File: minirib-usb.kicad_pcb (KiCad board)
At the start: 2 copper layers, 49.5 x 22.5 mm, 56 parts, among them J1 USB_B_Micro, J2 SB9600 Out, Q1 MMST3904-7-F, Q2 MMST3906-7-F, Q3 MMST3906-7-F, Q4 MMST3904-7-F, Q5 MMST3904-7-F, Q6 MMST3904-7-F, Q7 MMST3904-7-F, Q8 MMST3906-7-F, Q9 MMST3906-7-F, U1 CH340G, U2 TL081H, Y1 12MHz

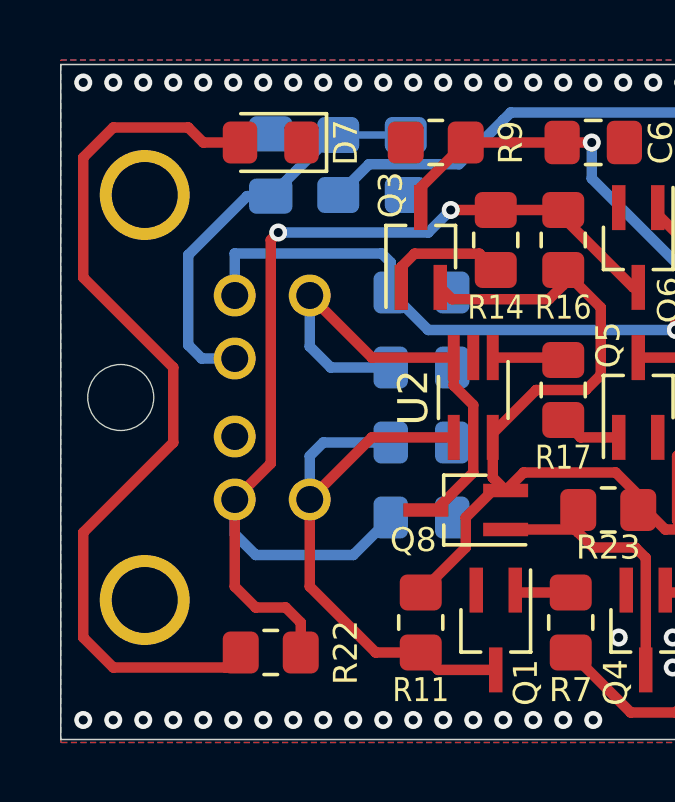
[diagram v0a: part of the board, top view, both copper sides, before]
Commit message: schematic fixes based on rev B testing
- switched Opamp to MCP6491T to use correct footprint (SC70 footprint for TL081H is incorrect)
- Removed D7 BUSY LED as it was interfering with the proper signalling on the BUSY line
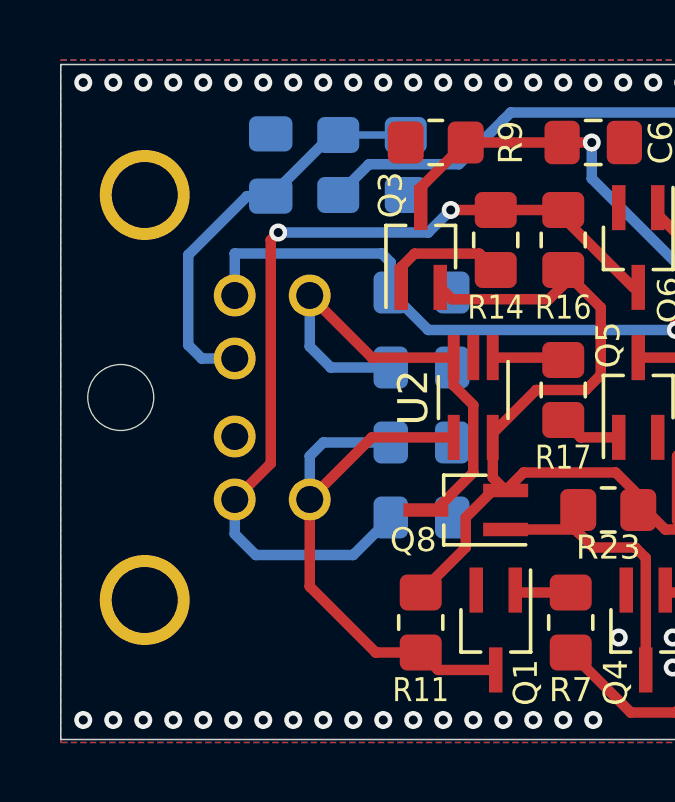
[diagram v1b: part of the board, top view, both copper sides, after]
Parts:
- removed D7: DLED, Diode_SMD:D_0805_2012Metric_Pad1.15x1.40mm_HandSolder
- removed R22: 1k5, Resistor_SMD:R_0805_2012Metric_Pad1.20x1.40mm_HandSolder
- C2, C9: value 0.1uF -> 22pF
- U2: value TL081H -> MCP6491T-E
- moved G*** 0.35 mm to (167.8, 108.5)
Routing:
- net Net-(D7-Pad2): track 30.2 -> 0.00 mm
- net BUSY: track 36.8 -> 30.2 mm

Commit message: finalized schematic and pcb
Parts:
- removed G***: LOGO, w3axl-logos:logo-4.2x4.2
- removed Q9: MMST3906-7-F, Package_TO_SOT_SMD:SOT-323_SC-70_Handsoldering
- removed Y1: 12MHz, Crystal:Crystal_SMD_SeikoEpson_FA238-4Pin_3.2x2.5mm_HandSoldering
- added D10: TXD, Diode_SMD:D_0805_2012Metric_Pad1.15x1.40mm_HandSolder, F.Cu at (165.5, 93.2)
- added D11: RXD, Diode_SMD:D_0805_2012Metric_Pad1.15x1.40mm_HandSolder, F.Cu at (165.5, 106.8)
- added D7: 1N4148, Diode_SMD:D_SOD-323_HandSoldering, F.Cu at (121.2, 93.8)
- added D8: PWR, Diode_SMD:D_0805_2012Metric_Pad1.15x1.40mm_HandSolder, F.Cu at (178.0, 92.5)
- added D9: BUSY, Diode_SMD:D_0805_2012Metric_Pad1.15x1.40mm_HandSolder, F.Cu at (117.0, 107.0)
- added J3: RS232, Connector_PinHeader_1.27mm:PinHeader_1x05_P1.27mm_Vertical, F.Cu at (154.5, 108.2)
- added R22: 1k5, Resistor_SMD:R_0805_2012Metric_Pad1.20x1.40mm_HandSolder, F.Cu at (114.2, 107.0)
- added U3: MAX232, Package_SO:SOIC-16W_7.5x10.3mm_P1.27mm, F.Cu at (152.0, 100.0)
- C2, C9: value 22pF -> 1uF; moved to F.Cu
- C5: value 220pF -> 0.1uF
- C6, C7, C8: value 220pF -> 1uF
- D5: value TXLED -> 1N4148; footprint Diode_SMD:D_0805_2012Metric_Pad1.15x1.40mm_HandSolder -> Diode_SMD:D_SOD-323_HandSoldering
- D6: value RXLED -> 1N4148; footprint Diode_SMD:D_0805_2012Metric_Pad1.15x1.40mm_HandSolder -> Diode_SMD:D_SOD-323_HandSoldering
- J2: value SB9600 Out -> Mini-DIN-6-Shielded
- Q1, Q5: value MMST3904-7-F -> MMBT3906; footprint Package_TO_SOT_SMD:SOT-323_SC-70_Handsoldering -> Package_TO_SOT_SMD:SOT-23
- Q2, Q3: value MMST3906-7-F -> MMBT3904; footprint Package_TO_SOT_SMD:SOT-323_SC-70_Handsoldering -> Package_TO_SOT_SMD:SOT-23
- Q4, Q6, Q7: value MMST3904-7-F -> MMBT3904; footprint Package_TO_SOT_SMD:SOT-323_SC-70_Handsoldering -> Package_TO_SOT_SMD:SOT-23
- Q8: value MMST3906-7-F -> BSS138W
- R10: value 4k7 -> 9k1
- R11: value 4k7 -> 47k
- R12: value 20k -> 10k
- R13, R19, R23, R24: value 4k7 -> 1k5
- R14, R15, R20: value 4k7 -> 10k
- R18: value 4k7 -> 20k
- R21: value 20k -> 1k5
- R3: value 3k -> 1k5; moved to F.Cu
- R4: value 1k5 -> 10k; moved to F.Cu
- R5: value 1k5 -> 10k
- R6: value 1k5 -> 39k; moved to B.Cu
- R7: value 4k7 -> 10k; moved to B.Cu
- R8: value 2k2 -> 20k
- R9: value 2k2 -> 9k1
- U1: value CH340G -> FT231XS; footprint Package_SO:SOIC-16_3.9x9.9mm_P1.27mm -> Package_SO:SSOP-20_3.9x8.7mm_P0.635mm
- U2: value MCP6491T-E -> TL071; footprint Package_TO_SOT_SMD:SOT-353_SC-70-5_Handsoldering -> Package_TO_SOT_SMD:SOT-23-5_HandSoldering
- moved D6 57.6 mm to (111.5, 106.0), turned to -90 degrees
- moved D5 57.2 mm to (112.8, 93.0)
- moved R6 52.2 mm to (111.2, 98.0)
- moved R21 36.0 mm to (125.2, 107.5), turned to 0 degrees
- moved R5 32.3 mm to (132.5, 99.0), turned to 180 degrees
- moved R7 30.0 mm to (111.2, 100.0), turned to 0 degrees
- moved Q4 29.7 mm to (115.0, 97.5)
- moved R10 29.6 mm to (118.2, 102.5), turned to 90 degrees
- moved D2 29.3 mm to (106.0, 93.2), turned to 90 degrees
- moved D3 29.1 mm to (106.0, 106.8), turned to -90 degrees
- moved R19 28.7 mm to (175.5, 92.5), turned to -90 degrees
- moved D1 27.4 mm to (108.5, 93.2), turned to 90 degrees
- moved Q7 27.1 mm to (127.5, 93.8), turned to 0 degrees
- moved D4 26.9 mm to (108.5, 106.8), turned to -90 degrees
- moved R8 25.4 mm to (125.8, 100.0), turned to -90 degrees
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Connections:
- C2 pad 2: GND -> Net-(C2-Pad2)
- C5 pad 1: TXD -> +5V
- C6 pad 1: ~{CTS} -> +5V
- C7 pad 1: RXD -> Net-(C7-Pad1)
- C7 pad 2: GND -> Net-(C7-Pad2)
- C8 pad 1: ~{DTR} -> +8V
- C9 pad 1: Net-(C9-Pad1) -> GND
- C9 pad 2: GND -> -8V
- D5 pad 1: TXD -> Net-(D5-Pad1)
- D5 pad 2: Net-(D5-Pad2) -> GND
- D6 pad 1: RXD -> Net-(D6-Pad1)
- D6 pad 2: Net-(D6-Pad2) -> GND
- Q1 pad 2: GND -> +8V
- Q1 pad 3: BUS+ -> RXD
- Q2 pad 2: +5V -> GND
- Q2 pad 3: RXD -> Net-(Q2-Pad3)
- Q3 pad 1: Net-(Q3-Pad1) -> Net-(D6-Pad1)
- Q3 pad 2: +5V -> GND
- Q3 pad 3: ~{CTS} -> BUS+
- Q4 pad 1: Net-(Q4-Pad1) -> Net-(D5-Pad1)
- Q4 pad 2: GND -> BUS-
- Q4 pad 3: Net-(Q4-Pad3) -> +5V
- Q5 pad 2: GND -> +8V
- Q5 pad 3: Net-(Q5-Pad3) -> CTS
- Q7 pad 1: Net-(Q7-Pad1) -> Net-(D7-Pad1)
- Q7 pad 2: GND -> ~{BUSY}
- Q7 pad 3: Net-(Q7-Pad3) -> +5V
- Q8 pad 1: Net-(Q4-Pad3) -> Net-(Q8-Pad1)
- Q8 pad 2: +5V -> GND
- Q8 pad 3: BUS- -> Net-(D9-Pad1)
- R10 pad 1: Net-(Q4-Pad1) -> Net-(D6-Pad1)
- R11 pad 1: BUS+ -> Net-(D5-Pad1)
- R11 pad 2: +5V -> GND
- R12 pad 1: GND -> +5V
- R12 pad 2: Net-(Q4-Pad1) -> BUS+
- R13 pad 1: Net-(Q5-Pad3) -> CTS
- R13 pad 2: Net-(Q2-Pad1) -> -8V
- R14 pad 1: Net-(Q3-Pad1) -> BUSY
- R14 pad 2: BUSY -> Net-(Q5-Pad1)
- R15 pad 1: Net-(Q5-Pad3) -> BUSY
- R16 pad 1: BUSY -> Net-(D7-Pad1)
- R16 pad 2: +5V -> DTR
- R17 pad 1: Net-(Q5-Pad1) -> Net-(Q6-Pad1)
- R17 pad 2: Net-(R17-Pad2) -> GND
- R18 pad 1: GND -> Net-(D7-Pad1)
- R18 pad 2: Net-(Q6-Pad1) -> GND
- R19 pad 1: ~{BUSY} -> Net-(D8-Pad2)
- R19 pad 2: Net-(Q6-Pad1) -> +5V
- R20 pad 1: Net-(Q7-Pad1) -> ~{BUSY}
- R20 pad 2: ~{DTR} -> Net-(Q6-Pad1)
- R21 pad 1: GND -> Net-(Q8-Pad1)
- R21 pad 2: Net-(Q7-Pad1) -> BUSY
- R23 pad 1: Net-(Q4-Pad3) -> Net-(D10-Pad2)
- R24 pad 1: Net-(Q7-Pad3) -> Net-(D11-Pad2)
- R3 pad 1: BIAS -> RXD
- R3 pad 2: +5V -> -8V
- R4 pad 1: GND -> Net-(Q1-Pad1)
- R4 pad 2: BIAS -> Net-(Q2-Pad3)
- R5 pad 2: Net-(D5-Pad2) -> Net-(Q2-Pad3)
- R6 pad 1: Net-(D6-Pad2) -> +5V
- R6 pad 2: +5V -> BIAS
- R7 pad 1: Net-(Q1-Pad1) -> BIAS
- R7 pad 2: TXD -> GND
- R8 pad 1: GND -> Net-(R8-Pad1)
- R8 pad 2: RXD -> Net-(Q2-Pad1)
- R9 pad 1: GND -> Net-(D5-Pad1)
- R9 pad 2: ~{CTS} -> TXD
- U1 pad 1: GND -> ~{DTR_TTL}
- U1 pad 10: unconnected-(U1-Pad10) -> ~{RXLED}
- U1 pad 11: ~{CTS} -> Net-(R1-Pad1)
- U1 pad 12: unconnected-(U1-Pad12) -> Net-(R2-Pad2)
- U1 pad 13: ~{DTR} -> Net-(C10-Pad1)
- U1 pad 14: unconnected-(U1-Pad14) -> Net-(C10-Pad1)
- U1 pad 15: unconnected-(U1-Pad15) -> +5V
- U1 pad 16: +5V -> GND
- U1 pad 2: TXD -> unconnected-(U1-Pad2)
- U1 pad 3: RXD -> Net-(C10-Pad1)
- U1 pad 4: Net-(C10-Pad1) -> RXD_TTL
- U1 pad 5: Net-(R1-Pad1) -> ~{CTS_TTL}
- U1 pad 6: Net-(R2-Pad2) -> GND
- U1 pad 7: Net-(C2-Pad1) -> unconnected-(U1-Pad7)
- U1 pad 8: Net-(C9-Pad1) -> unconnected-(U1-Pad8)
- U1 pad 9: ~{CTS} -> ~{CTS_TTL}
- U2 pad 1: Net-(R17-Pad2) -> Net-(R8-Pad1)
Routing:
- net +8V: track 0.00 -> 30.5 mm
- net ~{CTS}: track 29.4 -> 0.00 mm, vias 2 -> 0
- net BUSY: track 30.2 -> 58.3 mm
- net TXD: track 36.8 -> 61.4 mm
- net DTR: track 0.00 -> 23.3 mm, vias 0 -> 2
- net Net-(D7-Pad1): track 0.00 -> 22.4 mm
- net +5V: track 128.2 -> 146.1 mm, vias 1 -> 4
- net ~{DTR}: track 17.5 -> 0.00 mm
- net ~{BUSY}: track 25.1 -> 42.5 mm, vias 1 -> 0
- net CTS: track 0.00 -> 16.7 mm
- net TXD_TTL: track 0.00 -> 13.5 mm, vias 0 -> 2
- net -8V: track 0.00 -> 11.8 mm
- net ~{DTR_TTL}: track 0.00 -> 11.3 mm, vias 0 -> 2
- net ~{CTS_TTL}: track 0.00 -> 10.5 mm
- net Net-(C2-Pad1): track 12.9 -> 2.75 mm, vias 1 -> 0
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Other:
- board size 49.5 x 22.5 mm -> 79.5 x 23 mm
- board text removed: "MiniRIB USB rev B - 2022/01/04"

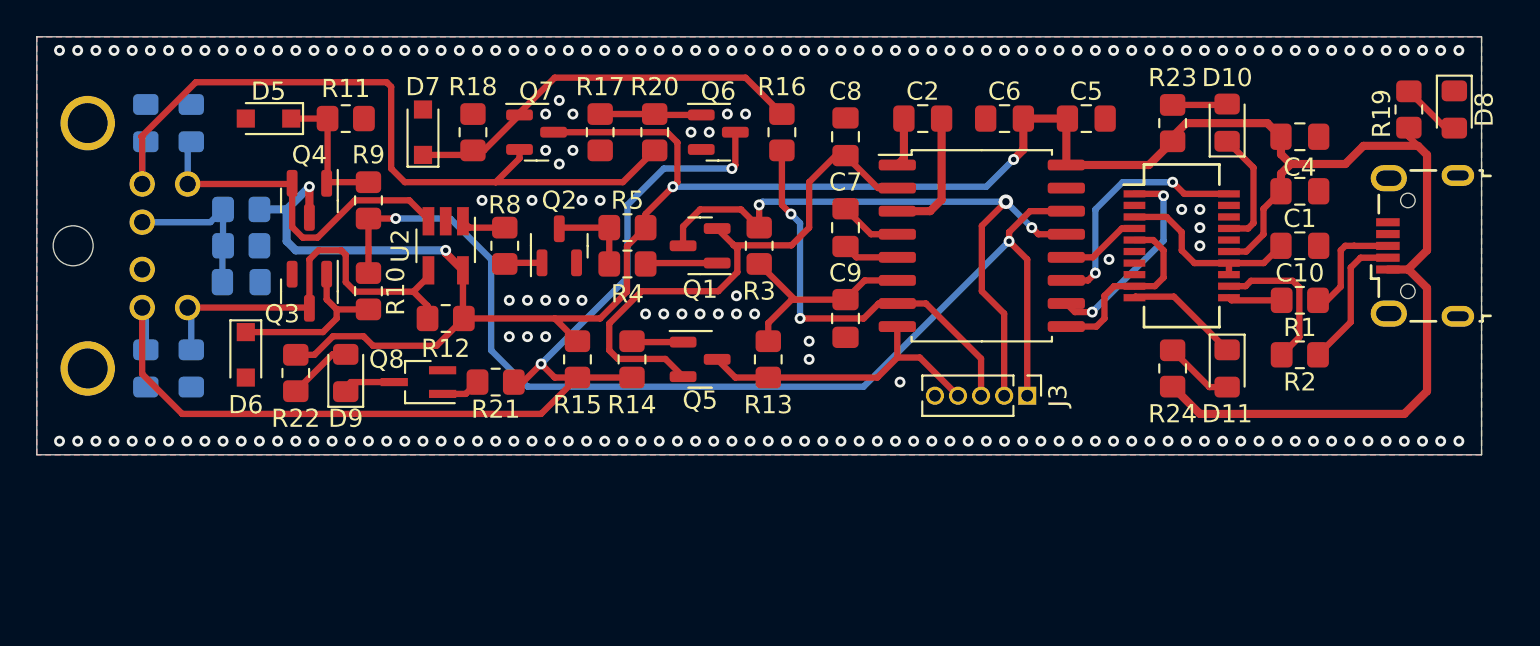
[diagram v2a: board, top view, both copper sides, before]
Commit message: generated schematic and gerbers for rev C PCB
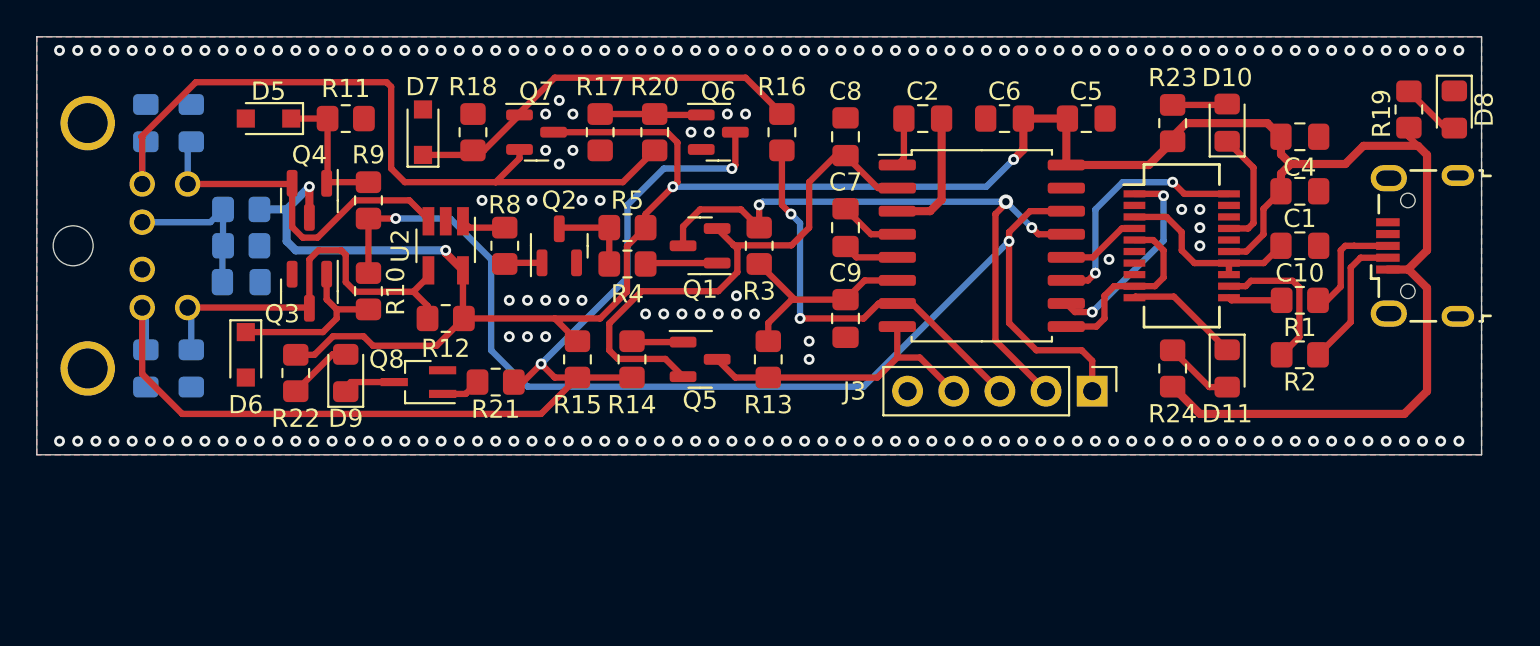
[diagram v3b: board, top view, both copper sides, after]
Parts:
- J3: footprint Connector_PinHeader_1.27mm:PinHeader_1x05_P1.27mm_Vertical -> Connector_PinHeader_2.54mm:PinHeader_1x05_P2.54mm_Vertical
- moved J3 3.58 mm to (158.1, 108.0)
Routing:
- net TXD: track 61.4 -> 64.1 mm
- net GND: vias 194 -> 193

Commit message: initial revision D updates
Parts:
- removed C10, C5: 0.1uF, Capacitor_SMD:C_0805_2012Metric_Pad1.18x1.45mm_HandSolder
- removed C6, C7, C8, C9: 1uF, Capacitor_SMD:C_0805_2012Metric_Pad1.18x1.45mm_HandSolder
- removed D10: TXD, Diode_SMD:D_0805_2012Metric_Pad1.15x1.40mm_HandSolder
- removed D11: RXD, Diode_SMD:D_0805_2012Metric_Pad1.15x1.40mm_HandSolder
- removed D9: BUSY, Diode_SMD:D_0805_2012Metric_Pad1.15x1.40mm_HandSolder
- removed Q8: BSS138W, Package_TO_SOT_SMD:SOT-323_SC-70_Handsoldering
- removed R19, R21, R22, R23, R24: 1k5, Resistor_SMD:R_0805_2012Metric_Pad1.20x1.40mm_HandSolder
- removed R20: 10k, Resistor_SMD:R_0805_2012Metric_Pad1.20x1.40mm_HandSolder
- removed U3: MAX232, Package_SO:SOIC-16W_7.5x10.3mm_P1.27mm
- added G***: LOGO, w3axl-logos:logo-6.3x6.3, B.Cu at (110.2, 115.8)
- added H1: MountingHole_Pad, MountingHole:MountingHole_2.7mm_M2.5_Pad_TopBottom, F.Cu at (156.8, 93.2)
- added H2: MountingHole_Pad, MountingHole:MountingHole_2.7mm_M2.5_Pad_TopBottom, F.Cu at (156.8, 116.8)
- added H3: MountingHole_Pad, MountingHole:MountingHole_2.7mm_M2.5_Pad_TopBottom, F.Cu at (103.2, 93.2)
- added H4: MountingHole_Pad, MountingHole:MountingHole_2.7mm_M2.5_Pad_TopBottom, F.Cu at (103.2, 116.8)
- added J4: UART, Connector_PinHeader_2.54mm:PinHeader_1x05_P2.54mm_Vertical, F.Cu at (125.0, 117.5)
- C2: value 1uF -> 0.1uF
- C3, D1, D2, D3, D4, R6, R7: moved to F.Cu
- D5: value 1N4148 -> PWR; footprint Diode_SMD:D_SOD-323_HandSoldering -> Diode_SMD:D_0805_2012Metric_Pad1.15x1.40mm_HandSolder
- D6: value 1N4148 -> BUSY; footprint Diode_SMD:D_SOD-323_HandSoldering -> Diode_SMD:D_0805_2012Metric_Pad1.15x1.40mm_HandSolder
- D7: value 1N4148 -> TXD; footprint Diode_SMD:D_SOD-323_HandSoldering -> Diode_SMD:D_0805_2012Metric_Pad1.15x1.40mm_HandSolder
- D8: value PWR -> RXD
- J3: value RS232 -> UART
- Q1: value MMBT3906 -> BS84W; footprint Package_TO_SOT_SMD:SOT-23 -> Package_TO_SOT_SMD:SOT-323_SC-70_Handsoldering
- Q2, Q4: value MMBT3904 -> BS84W; footprint Package_TO_SOT_SMD:SOT-23 -> Package_TO_SOT_SMD:SOT-323_SC-70_Handsoldering
- Q3, Q6, Q7: value MMBT3904 -> BSS138W; footprint Package_TO_SOT_SMD:SOT-23 -> Package_TO_SOT_SMD:SOT-323_SC-70_Handsoldering
- Q5: value MMBT3906 -> BSS138W; footprint Package_TO_SOT_SMD:SOT-23 -> Package_TO_SOT_SMD:SOT-323_SC-70_Handsoldering
- R10, R9: value 9k1 -> 10k
- R11: value 47k -> 10k
- R12, R14: value 10k -> 1k5
- R13, R3: value 1k5 -> 10k
- R16: value 4k7 -> 10k
- R17: value 4k7 -> 1k5
- R18: value 20k -> 1k5
- R8: value 20k -> 10k
- moved D8 42.0 mm to (142.5, 115.0)
- moved D5 38.6 mm to (151.2, 95.0), turned to 90 degrees
- moved R13 34.1 mm to (109.5, 91.5), turned to 0 degrees
- moved R18 29.9 mm to (145.0, 115.0)
- moved J3 27.8 mm to (135.0, 92.5)
- moved R12 27.8 mm to (148.8, 95.0), turned to -90 degrees
- moved R11 23.2 mm to (132.2, 110.5), turned to 90 degrees
- moved Q6 22.7 mm to (115.0, 96.8)
- moved R14 22.7 mm to (115.5, 91.5), turned to 0 degrees
- moved R5 22.1 mm to (117.8, 115.5), turned to 90 degrees
- moved Q4 22.1 mm to (135.8, 105.0)
- moved C4 21.9 mm to (149.3, 102.2)
- moved C1 21.6 mm to (149.3, 104.5)
- moved R9 21.4 mm to (138.5, 104.5)
- moved D7 21.3 mm to (142.5, 95.0)
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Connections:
- C2 pad 2: Net-(C2-Pad2) -> GND
- D5 pad 1: Net-(D5-Pad1) -> GND
- D5 pad 2: GND -> Net-(D5-Pad2)
- D6 pad 2: GND -> Net-(D6-Pad2)
- D7 pad 1: Net-(D7-Pad1) -> ~{TXLED}
- D7 pad 2: GND -> Net-(D7-Pad2)
- D8 pad 1: GND -> ~{RXLED}
- J3 pad 3: DTR -> BUSY
- J3 pad 4: CTS -> ~{DTR}
- Q1 pad 1: Net-(Q1-Pad1) -> TXD
- Q1 pad 2: +8V -> +5V
- Q1 pad 3: RXD -> BUS-
- Q2 pad 1: Net-(Q2-Pad1) -> TXD
- Q2 pad 2: GND -> +5V
- Q3 pad 1: Net-(D6-Pad1) -> Net-(Q2-Pad3)
- Q4 pad 1: Net-(D5-Pad1) -> ~{DTR}
- Q4 pad 2: BUS- -> +5V
- Q4 pad 3: +5V -> ~{BUSY}
- Q5 pad 1: Net-(Q5-Pad1) -> ~{BUSY}
- Q5 pad 2: +8V -> GND
- Q5 pad 3: CTS -> BUSY
- Q6 pad 3: BUSY -> Net-(D6-Pad1)
- Q7 pad 1: Net-(D7-Pad1) -> Net-(Q7-Pad1)
- Q7 pad 2: ~{BUSY} -> GND
- Q7 pad 3: +5V -> RXD
- R10 pad 1: Net-(D6-Pad1) -> GND
- R10 pad 2: TXD -> ~{BUSY}
- R11 pad 1: Net-(D5-Pad1) -> +5V
- R11 pad 2: GND -> BUSY
- R12 pad 1: +5V -> Net-(D5-Pad2)
- R12 pad 2: BUS+ -> +5V
- R13 pad 1: CTS -> ~{BUSY}
- R13 pad 2: -8V -> Net-(Q6-Pad1)
- R14 pad 1: BUSY -> Net-(D6-Pad2)
- R14 pad 2: Net-(Q5-Pad1) -> +5V
- R15 pad 1: BUSY -> Net-(Q7-Pad1)
- R15 pad 2: +5V -> GND
- R16 pad 1: Net-(D7-Pad1) -> RXD
- R16 pad 2: DTR -> +5V
- R17 pad 1: Net-(Q6-Pad1) -> Net-(D7-Pad2)
- R17 pad 2: GND -> +5V
- R18 pad 1: Net-(D7-Pad1) -> Net-(D8-Pad2)
- R18 pad 2: GND -> +5V
- R3 pad 1: RXD -> TXD
- R3 pad 2: -8V -> +5V
- R4 pad 1: Net-(Q1-Pad1) -> GND
- R5 pad 2: Net-(Q2-Pad3) -> BUS+
- R8 pad 1: Net-(R8-Pad1) -> GND
- R8 pad 2: Net-(Q2-Pad1) -> BUS-
- R9 pad 1: Net-(D5-Pad1) -> ~{DTR}
- R9 pad 2: TXD -> +5V
- U1 pad 1: ~{DTR_TTL} -> ~{DTR}
- U1 pad 13: Net-(C10-Pad1) -> Net-(C2-Pad1)
- U1 pad 14: Net-(C10-Pad1) -> Net-(C2-Pad1)
- U1 pad 20: TXD_TTL -> TXD
- U1 pad 3: Net-(C10-Pad1) -> Net-(C2-Pad1)
- U1 pad 4: RXD_TTL -> RXD
- U1 pad 5: ~{CTS_TTL} -> BUSY
- U1 pad 9: ~{CTS_TTL} -> BUSY
- U2 pad 1: Net-(R8-Pad1) -> Net-(Q7-Pad1)
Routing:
- net BUSY: track 58.3 -> 90.1 mm, vias 2 -> 1
- net +8V: track 30.5 -> 0.00 mm
- net ~{BUSY}: track 42.5 -> 72.9 mm, vias 0 -> 2
- net +5V: track 146.1 -> 173.8 mm, vias 4 -> 8
- net ~{DTR}: track 0.00 -> 23.4 mm, vias 0 -> 1
- net DTR: track 23.0 -> 0.00 mm, vias 2 -> 0
- net Net-(D7-Pad1): track 22.4 -> 0.00 mm
- net BUS-: track 19.7 -> 39.3 mm
- net CTS: track 16.7 -> 0.00 mm
- net TXD_TTL: track 13.5 -> 0.00 mm, vias 2 -> 0
- net BUS+: track 22.9 -> 36.3 mm
- net TXD: track 64.1 -> 51.2 mm
- net -8V: track 11.8 -> 0.00 mm
- net ~{DTR_TTL}: track 11.3 -> 0.00 mm, vias 2 -> 0
- net Net-(C10-Pad1): track 10.7 -> 0.00 mm
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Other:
- board size 79.5 x 23 mm -> 60 x 30 mm
- board text added: "MiniRIB USB Rev D"
